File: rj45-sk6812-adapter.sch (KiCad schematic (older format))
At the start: 7 parts, among them J1 RJ45, J2 Barrel_Jack, J3 Conn_01x08, J4 Conn_01x03, J5 Conn_01x03, J6 Conn_01x03, J7 Conn_01x03

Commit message: Added mini-USB socket
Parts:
- added J3: USB_B_Mini, Connector_USB:USB_Mini-B_Lumberg_2486_01_Horizontal, symbol Connector:USB_B_Mini
- renumbered J3 to J4, J4 to J5, J5 to J6, J6 to J7, J7 to J8
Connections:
- wire segments 46 -> 50
- no-connect marks 0 -> 3
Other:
- moved on the sheet: J1, J2, J4, J5, J6, J7, J8

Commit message: Finished layouting
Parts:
- added H1, H2: MountingHole, MountingHole:MountingHole_4.5mm, symbol Mechanical:MountingHole
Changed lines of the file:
@@
+	1    0    0    -1
+$EndComp
+$Comp
+L Mechanical:MountingHole H1
+U 1 1 5BD1E664
+P 5950 4600
+F 0 "H1" H 6050 4646 50  0000 L CNN
+F 1 "MountingHole" H 6050 4555 50  0000 L CNN
+F 2 "MountingHole:MountingHole_4.5mm" H 5950 4600 50  0001 C CNN
+F 3 "~" H 5950 4600 50  0001 C CNN
+	1    5950 4600
+	1    0    0    -1
+$EndComp
+$Comp
+L Mechanical:MountingHole H2
+U 1 1 5BD1E6D9
+P 5950 4850
+F 0 "H2" H 6050 4896 50  0000 L CNN
+F 1 "MountingHole" H 6050 4805 50  0000 L CNN
+F 2 "MountingHole:MountingHole_4.5mm" H 5950 4850 50  0001 C CNN
+F 3 "~" H 5950 4850 50  0001 C CNN
+	1    5950 4850
 	1    0    0    -1
 $EndComp

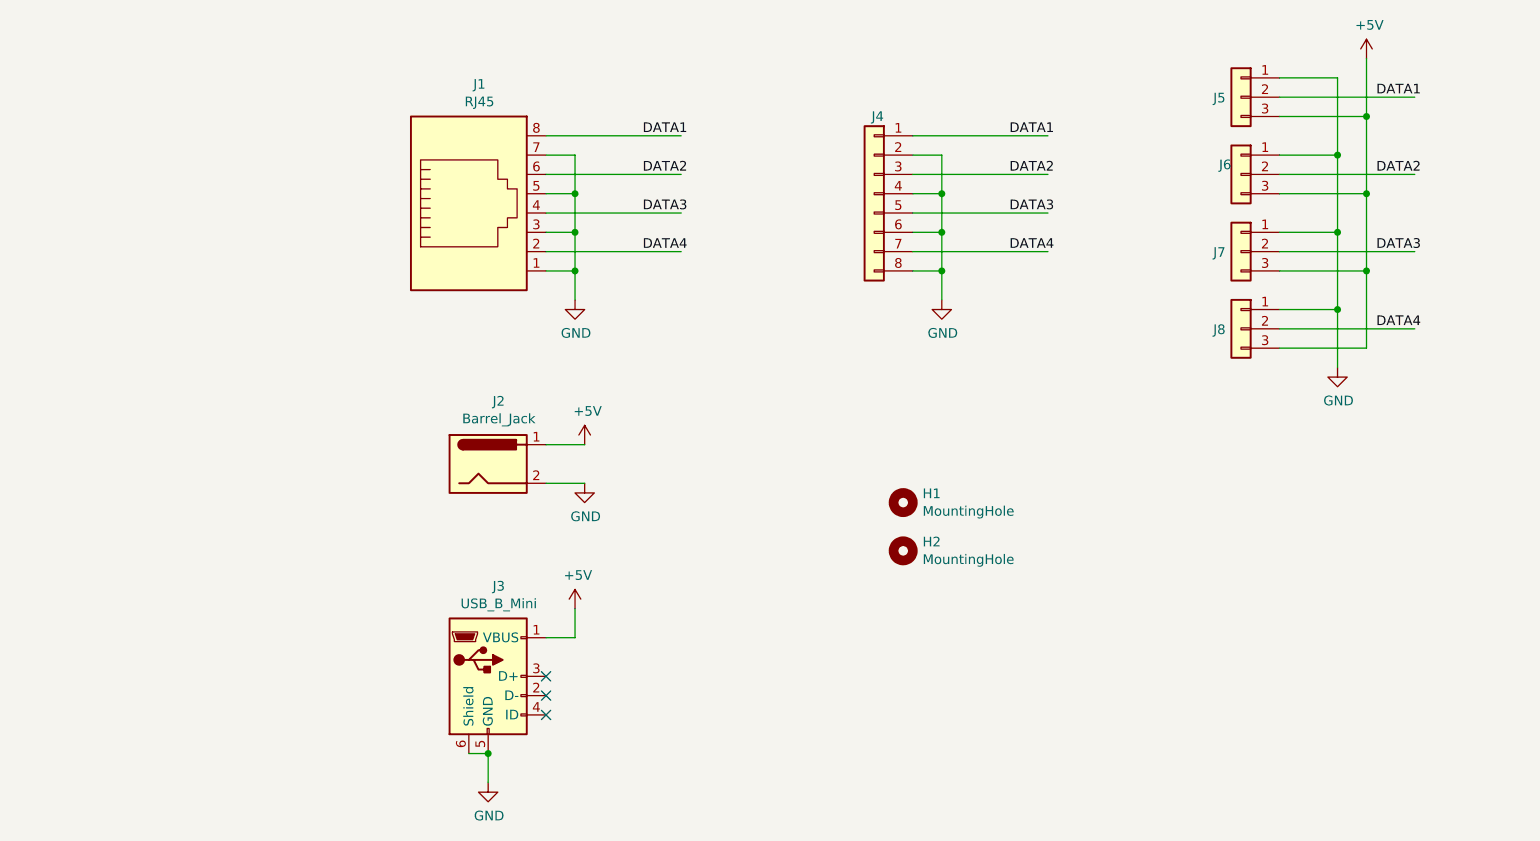
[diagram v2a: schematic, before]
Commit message: Using the correct RJ-45 socket
Added LED resistor and capacitor
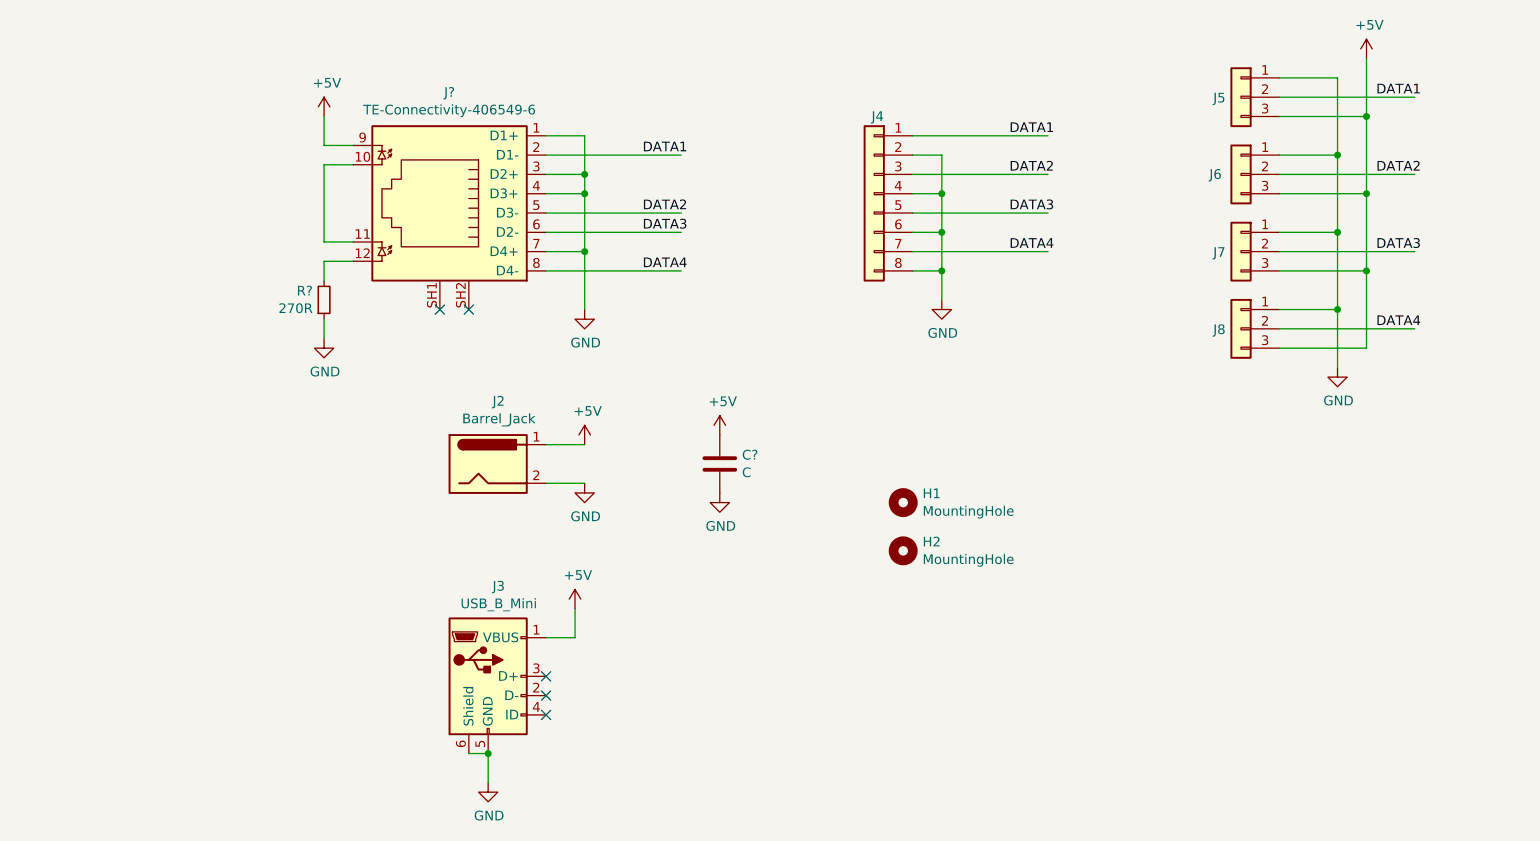
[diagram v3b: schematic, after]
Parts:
- removed J1: RJ45, Connector_RJ:RJ45_Amphenol_54602-x08_Horizontal, symbol Connector:RJ45
- added C?: C, Capacitor_SMD:C_0805_2012Metric_Pad1.15x1.40mm_HandSolder, symbol Device:C
- added J?: TE-Connectivity-406549-6, symbol Matthias:TE-Connectivity-406549-6
- added R?: 270R, Resistor_SMD:R_0805_2012Metric_Pad1.15x1.40mm_HandSolder, symbol Device:R_Small
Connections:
- wire segments 50 -> 58
- no-connect marks 3 -> 5
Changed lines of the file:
@@
 $EndDescr
-$Comp
-L Connector:RJ45 J1
-U 1 1 5BD1B190
-P 3700 3100
-F 0 "J1" H 3755 3767 50  0000 C CNN
-F 1 "RJ45" H 3755 3676 50  0000 C CNN
-F 2 "Connector_RJ:RJ45_Amphenol_54602-x08_Horizontal" V 3700 3125 50  0001 C CNN
-F 3 "~" V 3700 3125 50  0001 C CNN
-	1    3700 3100
-	1    0    0    -1
-$EndComp
 $Comp
 L Connector_Generic:Conn_01x08 J4
@@
 U 1 1 5BD1B545
 P 7700 2900
-F 0 "J6" H 7750 2950 50  0000 L CNN
+F 0 "J6" H 7800 2900 50  0000 L CNN
 F 1 "Conn_01x03" H 15980 6401 50  0001 L CNN
 F 2 "Connector_PinHeader_2.54mm:PinHeader_1x03_P2.54mm_Horizontal" H 7700 2900 50  0001 C CNN
@@
 L power:GND #PWR02
 U 1 1 5BD1B3BA
-P 4250 3550
-F 0 "#PWR02" H 4250 3300 50  0001 C CNN
-F 1 "GND" H 4255 3377 50  0000 C CNN
-F 2 "" H 4250 3550 50  0001 C CNN
-F 3 "" H 4250 3550 50  0001 C CNN
-	1    4250 3550
-	1    0    0    -1
-$EndComp
-Wire Wire Line
-	4100 2700 4800 2700
-Wire Wire Line
-	4100 2900 4800 2900
+P 4300 3600
+F 0 "#PWR02" H 4300 3350 50  0001 C CNN
+F 1 "GND" H 4305 3427 50  0000 C CNN
+F 2 "" H 4300 3600 50  0001 C CNN
+F 3 "" H 4300 3600 50  0001 C CNN
+	1    4300 3600
+	1    0    0    -1
+$EndComp
+Wire Wire Line
+	4100 2800 4800 2800
 Wire Wire Line
 	4100 3100 4800 3100
 Wire Wire Line
-	4100 3300 4800 3300
-Text Label 4600 2700 0    50   ~ 0
+	4100 3200 4800 3200
+Wire Wire Line
+	4100 3400 4800 3400
+Text Label 4600 2800 0    50   ~ 0
 DATA1
-Text Label 4600 2900 0    50   ~ 0
+Text Label 4600 3100 0    50   ~ 0
 DATA2
-Text Label 4600 3100 0    50   ~ 0
+Text Label 4600 3200 0    50   ~ 0
 DATA3
-Text Label 4600 3300 0    50   ~ 0
+Text Label 4600 3400 0    50   ~ 0
 DATA4
-Wire Wire Line
-	4250 3550 4250 3400
-Wire Wire Line
-	4250 2800 4100 2800
-Wire Wire Line
-	4250 3000 4100 3000
-Connection ~ 4250 3000
-Wire Wire Line
-	4250 3000 4250 2800
-Wire Wire Line
-	4100 3200 4250 3200
-Connection ~ 4250 3200
-Wire Wire Line
-	4250 3200 4250 3000
-Wire Wire Line
-	4250 3400 4100 3400
-Connection ~ 4250 3400
-Wire Wire Line
-	4250 3400 4250 3200
 $Comp
 L power:+5V #PWR04
@@
 	1    0    0    -1
 $EndComp
+NoConn ~ 3700 3600
+NoConn ~ 3550 3600
+Wire Wire Line
+	4100 3300 4300 3300
+Connection ~ 4300 3300
+Wire Wire Line
+	4300 3300 4300 3600
+Wire Wire Line
+	4100 3000 4300 3000
+Connection ~ 4300 3000
+Wire Wire Line
+	4300 3000 4300 3300
+Wire Wire Line
+	4100 2900 4300 2900
+Connection ~ 4300 2900
+Wire Wire Line
+	4300 2900 4300 3000
+Wire Wire Line
+	4300 2700 4100 2700
+Wire Wire Line
+	4300 2700 4300 2900
+$Comp
+L power:+5V #PWR?
+U 1 1 5BFDCD09
+P 5000 4250
+F 0 "#PWR?" H 5000 4100 50  0001 C CNN
+F 1 "+5V" H 5015 4423 50  0000 C CNN
+F 2 "" H 5000 4250 50  0001 C CNN
+F 3 "" H 5000 4250 50  0001 C CNN
+	1    5000 4250
+	1    0    0    -1
+$EndComp
+$Comp
+L power:GND #PWR?
+U 1 1 5BFDD80B
+P 5000 4550
+F 0 "#PWR?" H 5000 4300 50  0001 C CNN
+F 1 "GND" H 5005 4377 50  0000 C CNN
+F 2 "" H 5000 4550 50  0001 C CNN
+F 3 "" H 5000 4550 50  0001 C CNN
+	1    5000 4550
+	1    0    0    -1
+$EndComp
+$Comp
+L Device:C C?
+U 1 1 5BFDE31F
+P 5000 4400
+F 0 "C?" H 5115 4446 50  0000 L CNN
+F 1 "C" H 5115 4355 50  0000 L CNN
+F 2 "Capacitor_SMD:C_0805_2012Metric_Pad1.15x1.40mm_HandSolder" H 5038 4250 50  0001 C CNN
+F 3 "~" H 5000 4400 50  0001 C CNN
+	1    5000 4400
+	1    0    0    -1
+$EndComp
+Wire Wire Line
+	3100 3250 2950 3250
+Wire Wire Line
+	2950 3250 2950 2850
+Wire Wire Line
+	2950 2850 3100 2850
+Wire Wire Line
+	3100 2750 2950 2750
+Wire Wire Line
+	2950 2750 2950 2600
+$Comp
+L power:+5V #PWR?
+U 1 1 5BFE1B5A
+P 2950 2600
+F 0 "#PWR?" H 2950 2450 50  0001 C CNN
+F 1 "+5V" H 2965 2773 50  0000 C CNN
+F 2 "" H 2950 2600 50  0001 C CNN
+F 3 "" H 2950 2600 50  0001 C CNN
+	1    2950 2600
+	1    0    0    -1
+$EndComp
+$Comp
+L power:GND #PWR?
+U 1 1 5BFE1DAE
+P 2950 3750
+F 0 "#PWR?" H 2950 3500 50  0001 C CNN
+F 1 "GND" H 2955 3577 50  0000 C CNN
+F 2 "" H 2950 3750 50  0001 C CNN
+F 3 "" H 2950 3750 50  0001 C CNN
+	1    2950 3750
+	1    0    0    -1
+$EndComp
+$Comp
+L Matthias:TE-Connectivity-406549-6 J?
+U 1 1 5BFD4914
+P 3600 3100
+F 0 "J?" H 3600 3725 50  0000 C CNN
+F 1 "TE-Connectivity-406549-6" H 3600 3634 50  0000 C CNN
+F 2 "" V 3500 3175 50  0001 C CNN
+F 3 "~" V 3500 3175 50  0001 C CNN
+	1    3600 3100
+	1    0    0    -1
+$EndComp
+$Comp
+L Device:R_Small R?
+U 1 1 5BFE3D98
+P 2950 3550
+F 0 "R?" H 2892 3504 50  0000 R CNN
+F 1 "270R" H 2892 3595 50  0000 R CNN
+F 2 "Resistor_SMD:R_0805_2012Metric_Pad1.15x1.40mm_HandSolder" H 2950 3550 50  0001 C CNN
+F 3 "~" H 2950 3550 50  0001 C CNN
+	1    2950 3550
+	1    0    0    1
+$EndComp
+Wire Wire Line
+	2950 3450 2950 3350
+Wire Wire Line
+	2950 3350 3100 3350
+Wire Wire Line
+	2950 3750 2950 3650
 $EndSCHEMATC

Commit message: Finished layouting
Added an optional circuit to blink an LED during data transmission
and a diode protected and 5V regulated power supply connector.
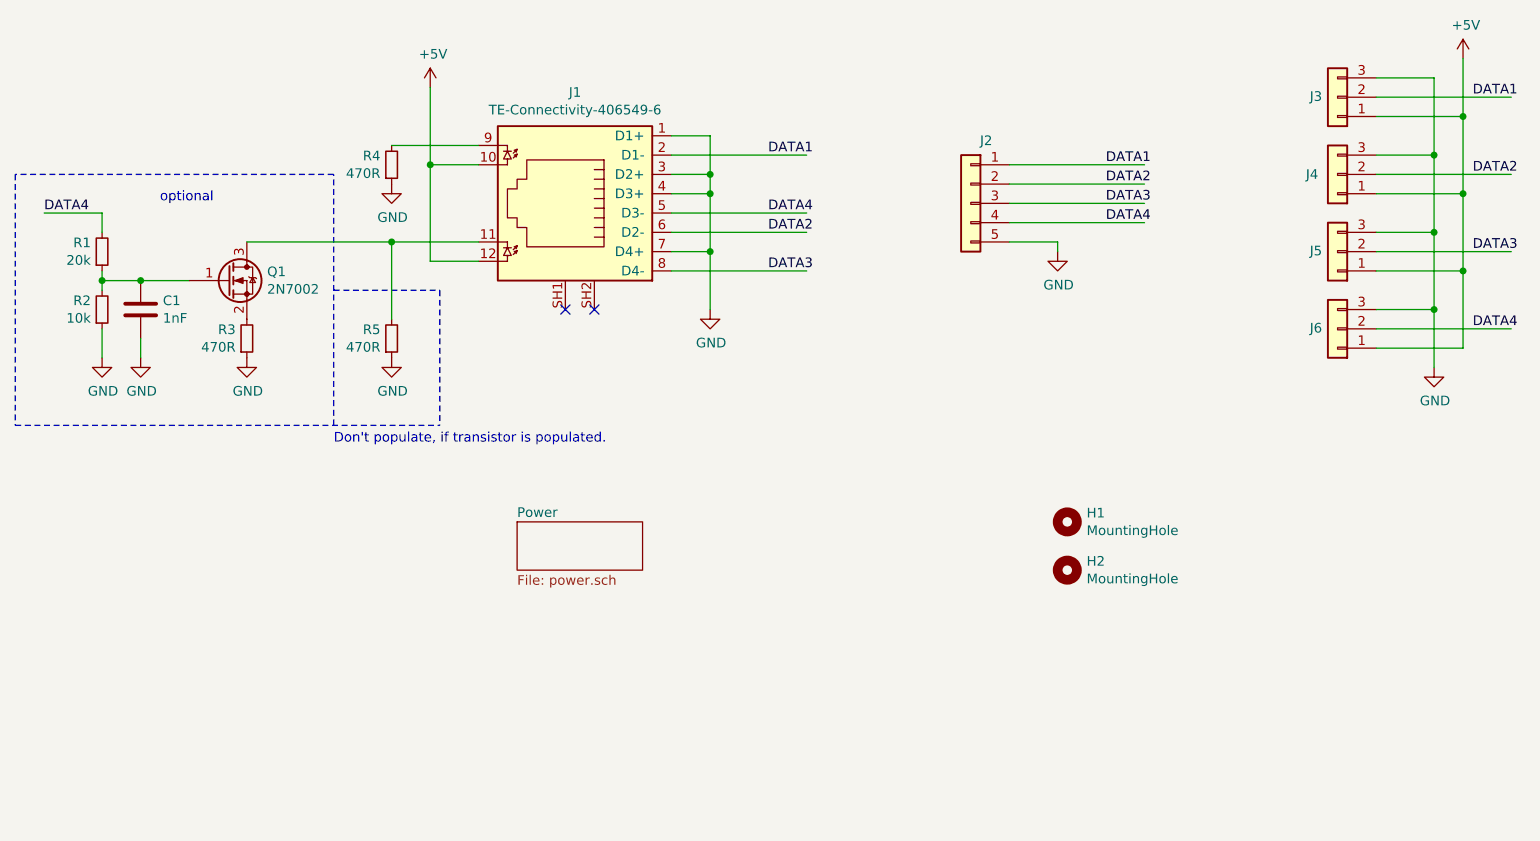
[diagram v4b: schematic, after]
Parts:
- removed C?: C, Capacitor_SMD:C_0805_2012Metric_Pad1.15x1.40mm_HandSolder, symbol Device:C
- removed J2: Barrel_Jack, Connector_BarrelJack:BarrelJack_CUI_PJ-102AH_Horizontal, symbol Connector:Barrel_Jack
- removed J3: USB_B_Mini, Connector_USB:USB_Mini-B_Lumberg_2486_01_Horizontal, symbol Connector:USB_B_Mini
- removed J4: Conn_01x08, Connector_PinHeader_2.54mm:PinHeader_1x08_P2.54mm_Vertical, symbol Connector_Generic:Conn_01x08
- added C1: 1nF, Capacitor_SMD:C_0805_2012Metric_Pad1.15x1.40mm_HandSolder, symbol Device:C
- added J2: Conn_01x05, Connector_PinHeader_2.54mm:PinHeader_1x05_P2.54mm_Vertical, symbol Connector_Generic:Conn_01x05
- added Q1: 2N7002, Package_TO_SOT_SMD:SOT-23, symbol Transistor_FET:2N7002
- added R1: 20k, Resistor_SMD:R_0805_2012Metric_Pad1.15x1.40mm_HandSolder, symbol Device:R_Small
- added R2: 10k, Resistor_SMD:R_0805_2012Metric_Pad1.15x1.40mm_HandSolder, symbol Device:R_Small
- added R3, R5: 470R, Resistor_SMD:R_0805_2012Metric_Pad1.15x1.40mm_HandSolder, symbol Device:R_Small
- J1: renamed from J?; footprint (none) -> Matthias:TE-Connectivity-406549-6
- J3: renamed from J5; footprint Connector_PinHeader_2.54mm:PinHeader_1x03_P2.54mm_Horizontal -> Matthias:WS6812-SK6812
- J4: renamed from J6; footprint Connector_PinHeader_2.54mm:PinHeader_1x03_P2.54mm_Horizontal -> Matthias:WS6812-SK6812
- J5: renamed from J7; footprint Connector_PinHeader_2.54mm:PinHeader_1x03_P2.54mm_Horizontal -> Matthias:WS6812-SK6812
- J6: renamed from J8; footprint Connector_PinHeader_2.54mm:PinHeader_1x03_P2.54mm_Horizontal -> Matthias:WS6812-SK6812
- R4: renamed from R?; value 270R -> 470R
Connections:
- wire segments 58 -> 54
- no-connect marks 5 -> 2
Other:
- note added: "Don't populate, if transistor is populated."
- note added: "optional"
- moved on the sheet: H1, H2, J1, J3, J4, J5, J6, R4
